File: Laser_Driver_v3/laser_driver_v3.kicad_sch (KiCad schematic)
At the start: 0 parts

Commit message: Worked on completing Controls and Drivers and CLK.
Laser and TEC drivers and controls now mostly complete.  Added a Clock that runs off an internal 10 MHz or switches to external 10 MHz.  Made minor changes elsewhere.
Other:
- removed sheet TEC Controller
- added sheet Clock (Clock.kicad_sch)
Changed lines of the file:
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@@
+	)
+	(sheet
+		(at 107.95 134.62)
+		(size 29.21 16.51)
+		(exclude_from_sim no)
+		(in_bom yes)
+		(on_board yes)
+		(dnp no)
+		(fields_autoplaced yes)
+		(stroke
+			(width 0.1524)
+			(type solid)
+		)
+		(fill
+			(color 0 0 0 0)
+		)
+		(property "Sheetname" "Clock"
+			(at 107.95 133.9084 0)
+			(show_name no)
+			(do_not_autoplace no)
+			(effects
+				(font
+					(size 1.27 1.27)
+				)
+				(justify left bottom)
+			)
+		)
+		(property "Sheetfile" "Clock.kicad_sch"
+			(at 107.95 151.7146 0)
+			(show_name no)
+			(do_not_autoplace no)
+			(effects
+				(font
+					(size 1.27 1.27)
+				)
+				(justify left top)
+			)
+		)
+		(instances
+			(project "laser_driver_v3"
+				(path "/b2c3d4e5-f6a7-8901-bcde-f12345678901"
+					(page "12")
+				)
+			)
+		)
 	)
 	(sheet
@@
 				(path "/b2c3d4e5-f6a7-8901-bcde-f12345678901"
 					(page "4")
-				)
-			)
-		)
-	)
-	(sheet
-		(at 138.43 64.77)
-		(size 22.86 27.94)
-		(exclude_from_sim no)
-		(in_bom yes)
-		(on_board yes)
-		(dnp no)
-		(fields_autoplaced yes)
-		(stroke
-			(width 0.1524)
-			(type solid)
-		)
-		(fill
-			(color 0 0 0 0)
-		)
-		(property "Sheetname" "TEC Controller"
-			(at 138.43 64.0584 0)
-			(show_name no)
-			(do_not_autoplace no)
-			(effects
-				(font
-					(size 1.27 1.27)
-				)
-				(justify left bottom)
-			)
-		)
-		(property "Sheetfile" "TEC Controller.kicad_sch"
-			(at 138.43 93.2946 0)
-			(show_name no)
-			(do_not_autoplace no)
-			(effects
-				(font
-					(size 1.27 1.27)
-				)
-				(justify left top)
-			)
-		)
-		(instances
-			(project "laser_driver_v3"
-				(path "/b2c3d4e5-f6a7-8901-bcde-f12345678901"
-					(page "9")
 				)
 			)
@@
 			(project "laser_driver_v3"
 				(path "/b2c3d4e5-f6a7-8901-bcde-f12345678901"
-					(page "12")
-				)
-			)
+					(page "9")
+				)
+			)

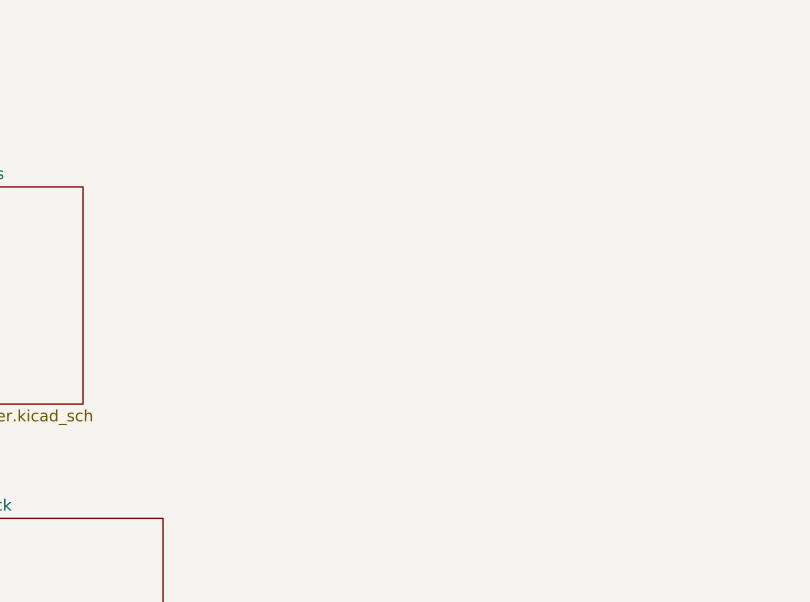
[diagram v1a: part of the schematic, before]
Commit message: Added DFB package sheet with pinout.  Minor update
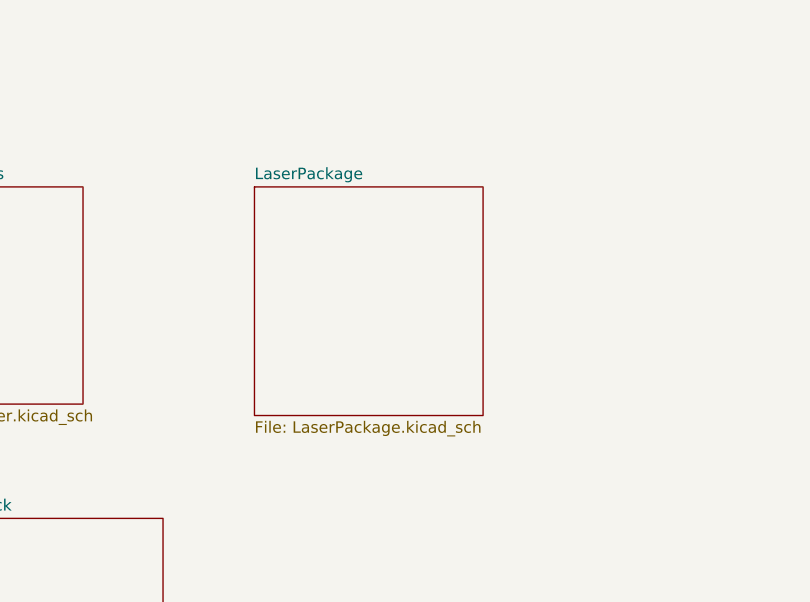
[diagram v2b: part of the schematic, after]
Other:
- added sheet LaserPackage (LaserPackage.kicad_sch)
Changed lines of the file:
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@@
+	)
+	(sheet
+		(at 143.51 67.31)
+		(size 25.4 25.4)
+		(exclude_from_sim no)
+		(in_bom yes)
+		(on_board yes)
+		(dnp no)
+		(fields_autoplaced yes)
+		(stroke
+			(width 0.1524)
+			(type solid)
+		)
+		(fill
+			(color 0 0 0 0)
+		)
+		(property "Sheetname" "LaserPackage"
+			(at 143.51 66.5984 0)
+			(show_name no)
+			(do_not_autoplace no)
+			(effects
+				(font
+					(size 1.27 1.27)
+				)
+				(justify left bottom)
+			)
+		)
+		(property "Sheetfile" "LaserPackage.kicad_sch"
+			(at 143.51 93.2946 0)
+			(show_name no)
+			(do_not_autoplace no)
+			(effects
+				(font
+					(size 1.27 1.27)
+				)
+				(justify left top)
+			)
+		)
+		(instances
+			(project "laser_driver_v3"
+				(path "/b2c3d4e5-f6a7-8901-bcde-f12345678901"
+					(page "13")
+				)
+			)
+		)
 	)
 	(sheet

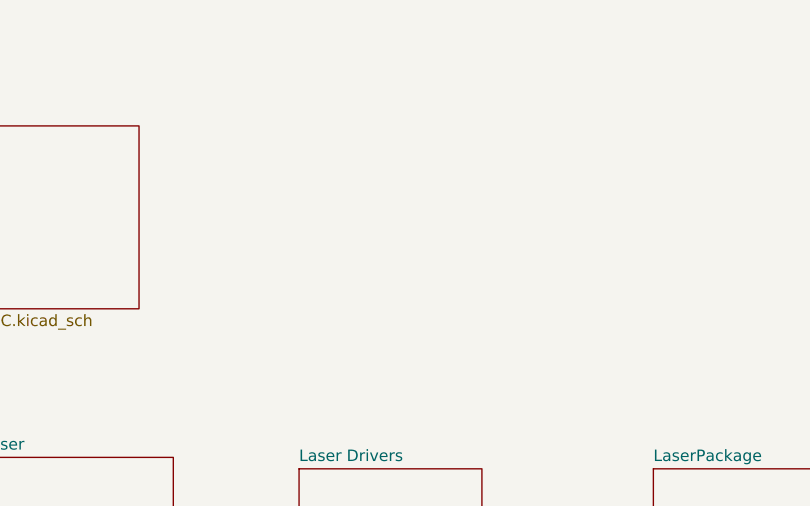
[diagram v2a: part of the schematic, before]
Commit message: First full draft complete.  Added Teensy pinout sheet.
Used Copilot to generate firmware draft.  ** Still need to:  Recheck all specifications and pins, verify design with simulations, go through all footprints, create layout.
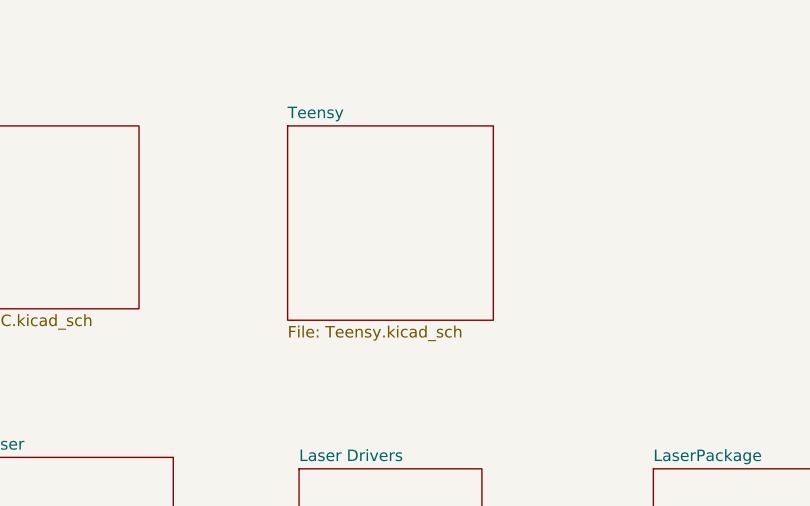
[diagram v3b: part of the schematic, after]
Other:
- added sheet Teensy (Teensy.kicad_sch)
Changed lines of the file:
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@@
+	)
+	(sheet
+		(at 102.87 29.21)
+		(size 22.86 21.59)
+		(exclude_from_sim no)
+		(in_bom yes)
+		(on_board yes)
+		(dnp no)
+		(fields_autoplaced yes)
+		(stroke
+			(width 0.1524)
+			(type solid)
+		)
+		(fill
+			(color 0 0 0 0)
+		)
+		(property "Sheetname" "Teensy"
+			(at 102.87 28.4984 0)
+			(show_name no)
+			(do_not_autoplace no)
+			(effects
+				(font
+					(size 1.27 1.27)
+				)
+				(justify left bottom)
+			)
+		)
+		(property "Sheetfile" "Teensy.kicad_sch"
+			(at 102.87 51.3846 0)
+			(show_name no)
+			(do_not_autoplace no)
+			(effects
+				(font
+					(size 1.27 1.27)
+				)
+				(justify left top)
+			)
+		)
+		(instances
+			(project "laser_driver_v3"
+				(path "/b2c3d4e5-f6a7-8901-bcde-f12345678901"
+					(page "14")
+				)
+			)
+		)
 	)
 	(sheet

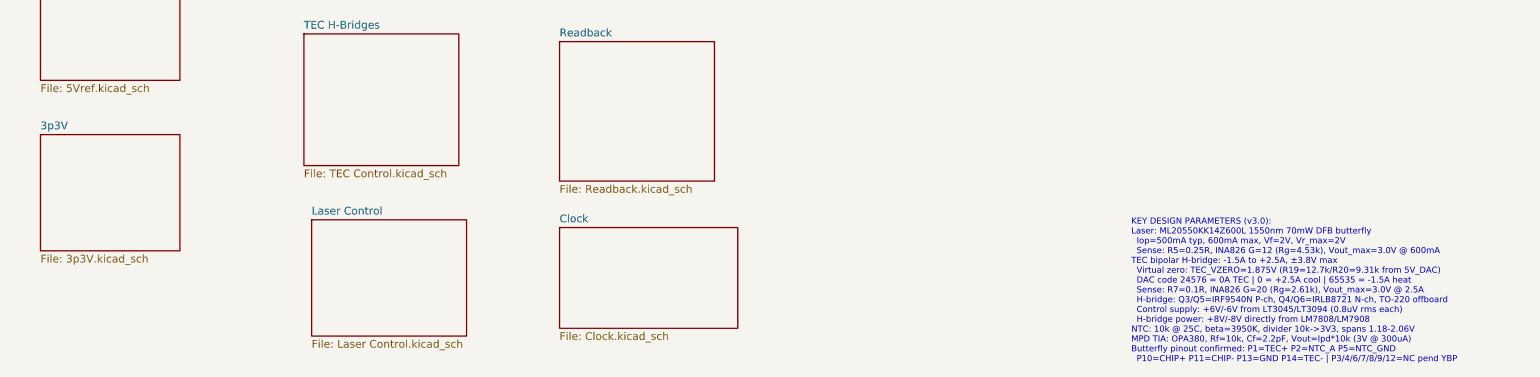
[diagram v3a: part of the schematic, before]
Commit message: Renumbered schematics, corrections, power verified
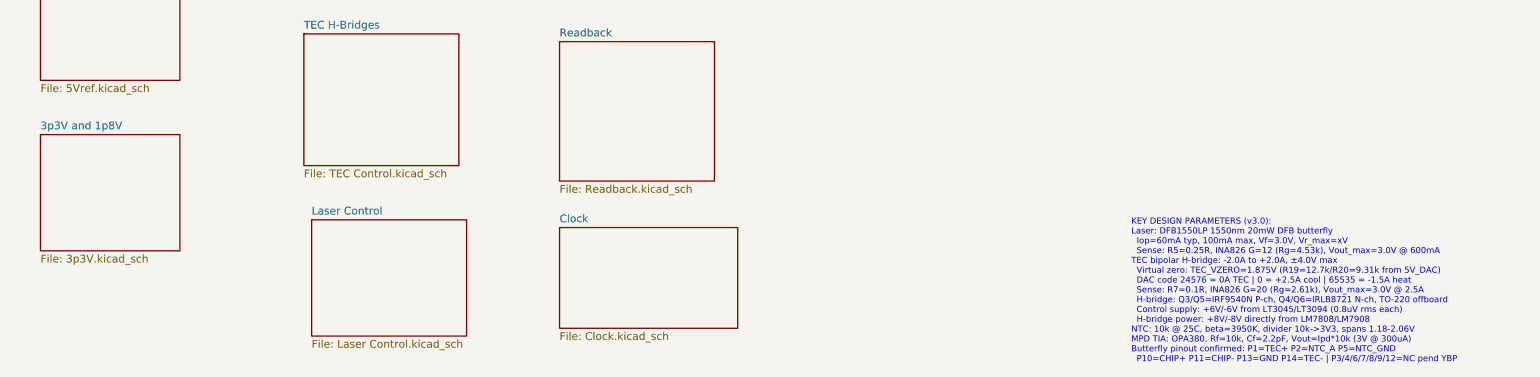
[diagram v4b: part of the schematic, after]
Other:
- sheet 3p3V renamed 3p3V and 1p8V
- note added: "KEY DESIGN PARAMETERS (v3.0): Laser: DFB1550LP 1550nm 20mW DFB butterfly Iop=60mA typ, 100mA max, Vf=3.0V, Vr_max=xV Sense: R5=0.25R, INA826 G=12 (Rg=4.53k), Vout_max=3.0V @ 600mA TEC bipolar H-bridge: -2.0A to +2.0A, ±4.0V max Virtual zero: TEC_VZERO=1.875V (R19=12.7k/R20=9.31k from 5V_DAC) DAC code 24576 = 0A TEC | 0 = +2.5A cool | 65535 = -1.5A heat Sense: R7=0.1R, INA826 G=20 (Rg=2.61k), Vout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"
- note removed: "KEY DESIGN PARAMETERS (v3.0): Laser: ML20550KK14Z600L 1550nm 70mW DFB butterfly Iop=500mA typ, 600mA max, Vf=2V, Vr_max=2V Sense: R5=0.25R, INA826 G=12 (Rg=4.53k), Vout_max=3.0V @ 600mA TEC bipolar H-bridge: -1.5A to +2.5A, ±3.8V max Virtual zero: TEC_VZERO=1.875V (R19=12.7k/R20=9.31k from 5V_DAC) DAC code 24576 = 0A TEC | 0 = +2.5A cool | 65535 = -1.5A heat Sense: R7=0.1R, INA826 G=20 (Rg=2.61k)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"
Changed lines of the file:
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@@
 		)
 	)
-	(text "KEY DESIGN PARAMETERS (v3.0):\nLaser: ML20550KK14Z600L 1550nm 70mW DFB butterfly\n  Iop=500mA typ, 600mA max, Vf=2V, Vr_max=2V\n  Sense: R5=0.25R, INA826 G=12 (Rg=4.53k), Vout_max=3.0V @ 600mA\nTEC bipolar H-bridge: -1.5A to +2.5A, ±3.8V max\n  Virtual zero: TEC_VZERO=1.875V (R19=12.7k/R20=9.31k from 5V_DAC)\n  DAC code 24576 = 0A TEC | 0 = +2.5A cool | 65535 = -1.5A heat\n  Sense: R7=0.1R, INA826 G=20 (Rg=2.61k), Vout_max=3.0V @ 2.5A\n  H-bridge: Q3/Q5=IRF9540N P-ch, Q4/Q6=IRLB8721 N-ch, TO-220 offboard\n  Control supply: +6V/-6V from LT3045/LT3094 (0.8uV rms each)\n  H-bridge power: +8V/-8V directly from LM7808/LM7908\nNTC: 10k @ 25C, beta=3950K, divider 10k->3V3, spans 1.18-2.06V\nMPD TIA: OPA380, Rf=10k, Cf=2.2pF, Vout=Ipd*10k (3V @ 300uA)\nButterfly pinout confirmed: P1=TEC+ P2=NTC_A P5=NTC_GND\n  P10=CHIP+ P11=CHIP- P13=GND P14=TEC- | P3/4/6/7/8/9/12=NC pend YBP"
+	(text "KEY DESIGN PARAMETERS (v3.0):\nLaser: DFB1550LP 1550nm 20mW DFB butterfly\n  Iop=60mA typ, 100mA max, Vf=3.0V, Vr_max=xV\n  Sense: R5=0.25R, INA826 G=12 (Rg=4.53k), Vout_max=3.0V @ 600mA\nTEC bipolar H-bridge: -2.0A to +2.0A, ±4.0V max\n  Virtual zero: TEC_VZERO=1.875V (R19=12.7k/R20=9.31k from 5V_DAC)\n  DAC code 24576 = 0A TEC | 0 = +2.5A cool | 65535 = -1.5A heat\n  Sense: R7=0.1R, INA826 G=20 (Rg=2.61k), Vout_max=3.0V @ 2.5A\n  H-bridge: Q3/Q5=IRF9540N P-ch, Q4/Q6=IRLB8721 N-ch, TO-220 offboard\n  Control supply: +6V/-6V from LT3045/LT3094 (0.8uV rms each)\n  H-bridge power: +8V/-8V directly from LM7808/LM7908\nNTC: 10k @ 25C, beta=3950K, divider 10k->3V3, spans 1.18-2.06V\nMPD TIA: OPA380, Rf=10k, Cf=2.2pF, Vout=Ipd*10k (3V @ 300uA)\nButterfly pinout confirmed: P1=TEC+ P2=NTC_A P5=NTC_GND\n  P10=CHIP+ P11=CHIP- P13=GND P14=TEC- | P3/4/6/7/8/9/12=NC pend YBP"
 		(exclude_from_sim no)
 		(at 201.676 145.034 0)
@@
 			(color 0 0 0 0)
 		)
-		(property "Sheetname" "3p3V"
+		(property "Sheetname" "3p3V and 1p8V"
 			(at 22.86 118.6684 0)
 			(show_name no)

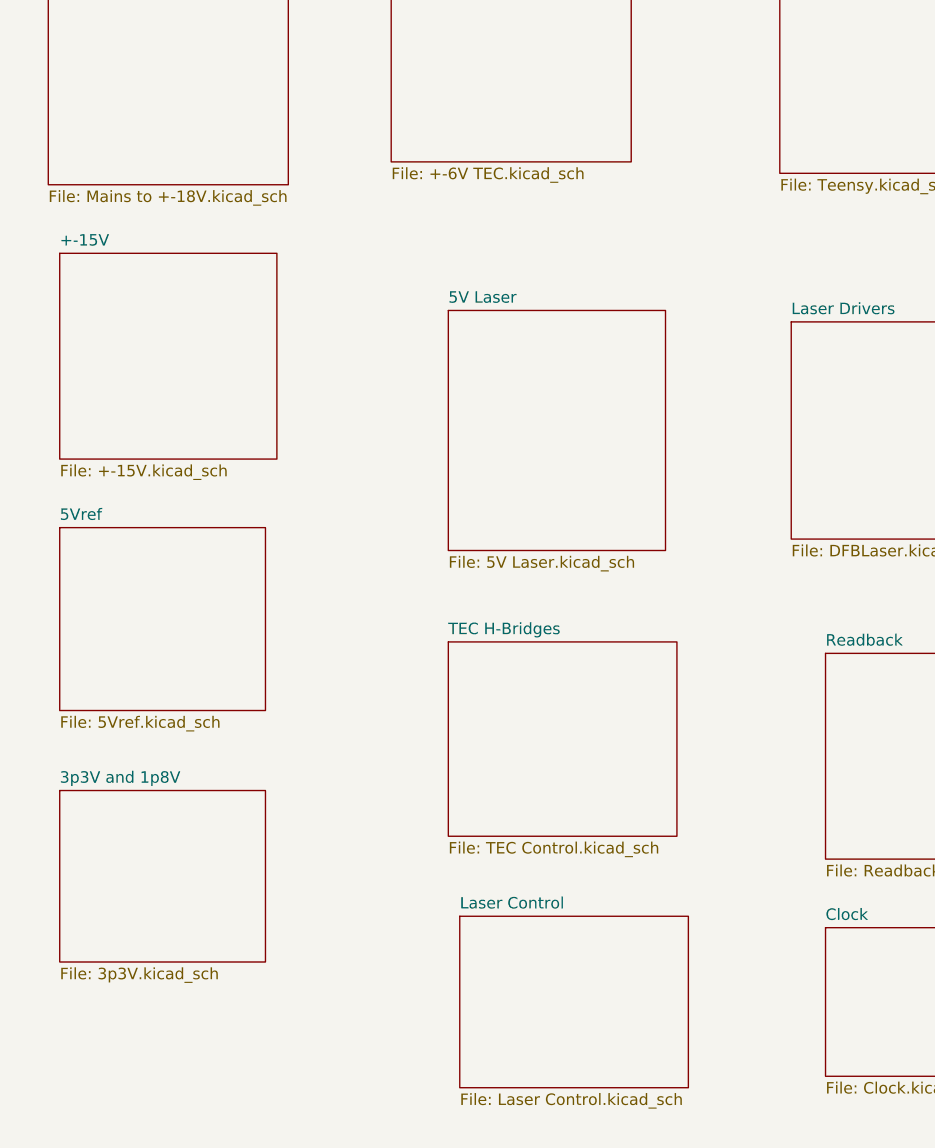
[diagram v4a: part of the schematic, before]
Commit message: Update names, footprints, values, and created BOM
Updated files names, foot prints, component values, parts.
Assigned values from Digikey catalog.
Created CSV BOMs for each schematic.
Including a Power analysis now for all components.
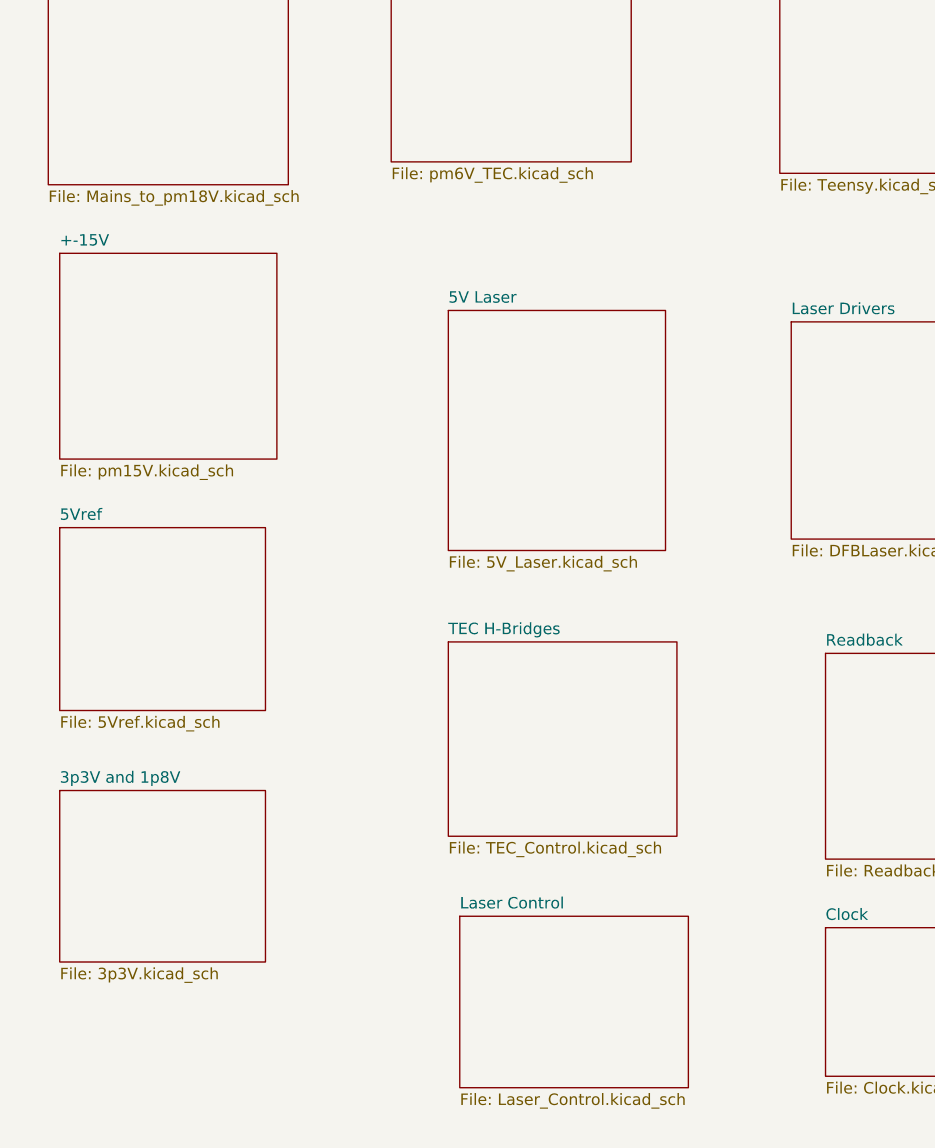
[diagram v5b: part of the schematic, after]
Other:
- sheet +-15V: file +-15V.kicad_sch -> pm15V.kicad_sch
- sheet +-6V TEC: file +-6V TEC.kicad_sch -> pm6V_TEC.kicad_sch
- sheet 5V Laser: file 5V Laser.kicad_sch -> 5V_Laser.kicad_sch
- sheet Laser Control: file Laser Control.kicad_sch -> Laser_Control.kicad_sch
- sheet Mains to +-18V: file Mains to +-18V.kicad_sch -> Mains_to_pm18V.kicad_sch
- sheet TEC H-Bridges: file TEC Control.kicad_sch -> TEC_Control.kicad_sch
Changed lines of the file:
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@@
 			)
 		)
-		(property "Sheetfile" "Mains to +-18V.kicad_sch"
+		(property "Sheetfile" "Mains_to_pm18V.kicad_sch"
 			(at 21.59 52.6546 0)
 			(show_name no)
@@
 			)
 		)
-		(property "Sheetfile" "TEC Control.kicad_sch"
+		(property "Sheetfile" "TEC_Control.kicad_sch"
 			(at 66.04 125.0446 0)
 			(show_name no)
@@
 			)
 		)
-		(property "Sheetfile" "+-6V TEC.kicad_sch"
+		(property "Sheetfile" "pm6V_TEC.kicad_sch"
 			(at 59.69 50.1146 0)
 			(show_name no)
@@
 			)
 		)
-		(property "Sheetfile" "5V Laser.kicad_sch"
+		(property "Sheetfile" "5V_Laser.kicad_sch"
 			(at 66.04 93.2946 0)
 			(show_name no)
@@
 			)
 		)
-		(property "Sheetfile" "+-15V.kicad_sch"
+		(property "Sheetfile" "pm15V.kicad_sch"
 			(at 22.86 83.1346 0)
 			(show_name no)
@@
 			)
 		)
-		(property "Sheetfile" "Laser Control.kicad_sch"
+		(property "Sheetfile" "Laser_Control.kicad_sch"
 			(at 67.31 152.9846 0)
 			(show_name no)

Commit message: Changed xfrmers, paralled BJTs for cap multiplier
Changed the transformers to more appropriate voltages.
Made the BJTs for the cap multipliers in parallel to better handle the load.
Simulated the output ripple for the 6V.
Clarifying notes, removed LT1028 changed to OPA192 to match circuit as drawn.
Changed divider values for the TEC_zero value to be 1.2 V as designed.
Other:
- company: Lab R&D -> Stefan Cular
- title: Dual Channel CW Laser + TEC Driver — ML20550KK14Z600L -> Dual Channel CW Laser + TEC Driver — DFB1550LP
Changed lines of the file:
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@@
 	(paper "USLetter")
 	(title_block
-		(title "Dual Channel CW Laser + TEC Driver — ML20550KK14Z600L")
+		(title "Dual Channel CW Laser + TEC Driver — DFB1550LP")
 		(date "2025-05-22")
 		(rev "3.0")
-		(company "Lab R&D")
+		(company "Stefan Cular")
 		(comment 1 "1550nm 70mW DFB butterfly | Bipolar TEC H-bridge -1.5A/+2.5A | AD5064 16-bit DAC")
 		(comment 2 "Rail2: LM7807->LT3042->LTC6655-5 | Rail3: LM7805->RC->LT3045 | Rail4/5: ±LM780x->LT3045/94")
